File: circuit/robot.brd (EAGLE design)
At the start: 90 x 70 mm, 31 parts, among them M1 SERVO-FLIPPED, M2 SERVO-1, U5 NANO, X1 NANO-HEADER-SURROUND, X2 NANO-HEADER-SURROUND

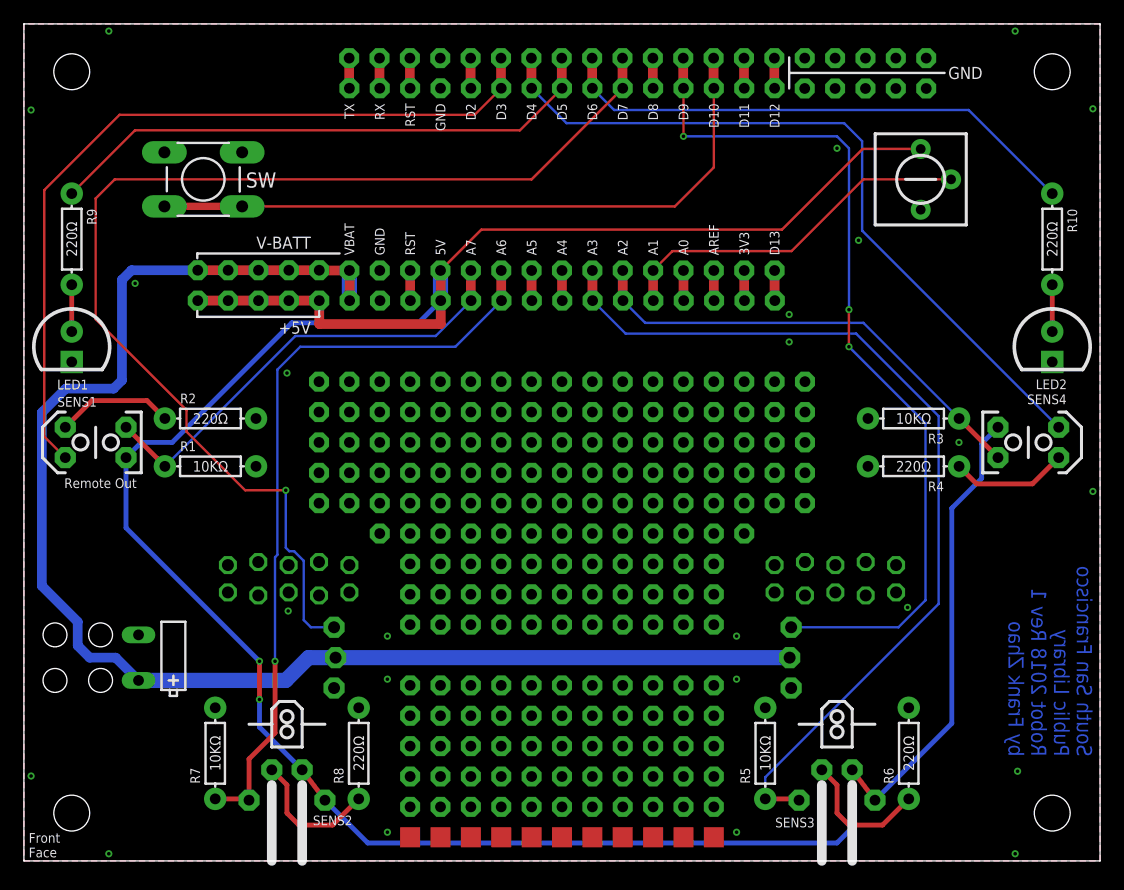
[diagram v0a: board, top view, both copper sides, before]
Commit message: circuit error: flipped floor sensor footprint
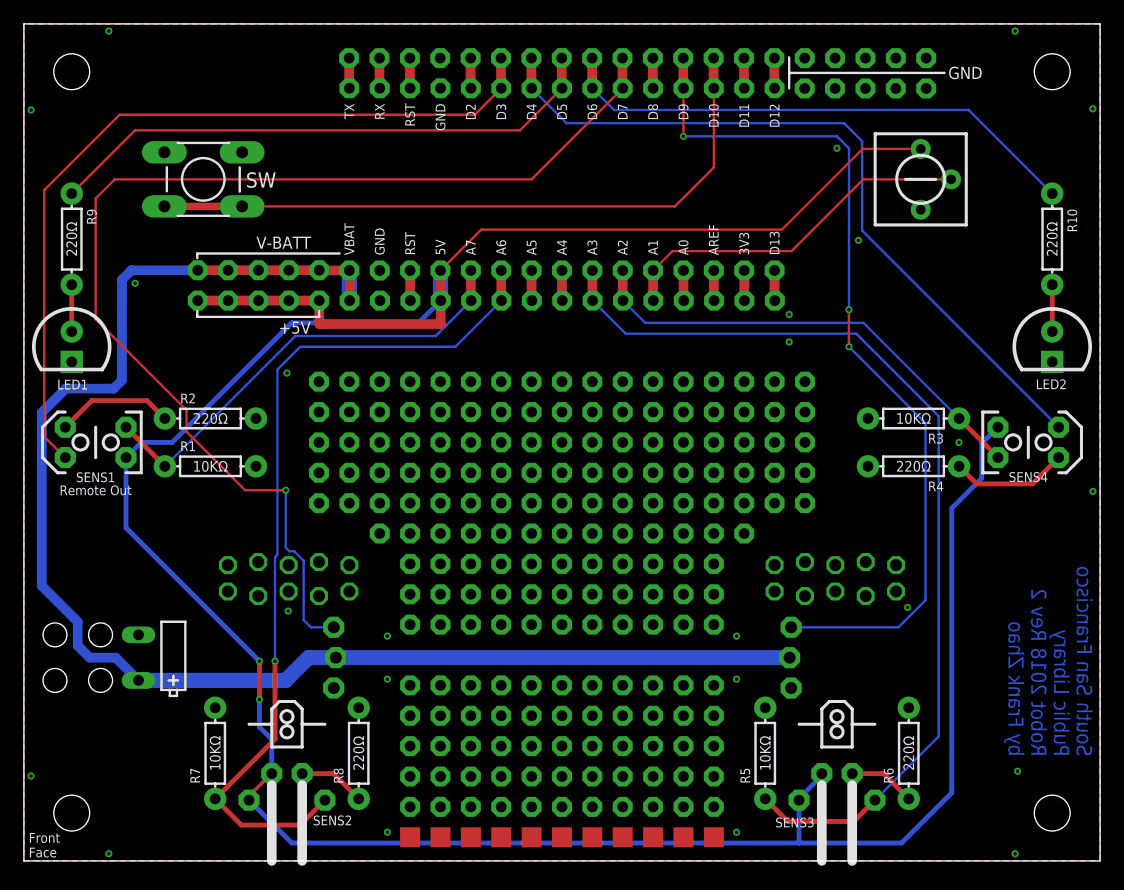
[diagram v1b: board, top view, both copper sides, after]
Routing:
- net 5V: track 230.4 -> 240.8 mm
- net SENS-RIGHT-FLOOR: track 63.5 -> 72.7 mm
- net N$4: track 11.5 -> 5.61 mm
- net N$3: track 11.5 -> 5.61 mm
- net SENS-LEFT-FLOOR: track 76.4 -> 80.5 mm
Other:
- board text added: "PROG"
